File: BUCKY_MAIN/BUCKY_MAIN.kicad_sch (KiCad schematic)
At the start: 17 parts, among them J4 Conn_01x10, U1 IFX9201SG_BO, U2 IFX9201SG_BO, U3 IFX9201SG_BO, U9 PCA9548ADB

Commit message: chore: finish main board
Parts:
- removed J4: Conn_01x10, BUCKY_MAIN:CONN10_S10B-PH_JST, symbol Connector_Generic:Conn_01x10
- removed R1, R2: 4700R, Resistor_SMD:R_0402_1005Metric, symbol Device:R
- removed R3, R4, R5, R6: 10000R, Resistor_SMD:R_0402_1005Metric, symbol Device:R
- removed U1, U2, U3: IFX9201SG_BO, BUCKY_MAIN:IFX9201SG_BO, symbol BUCKY_MAIN:IFX9201SG_BO
- removed U4: ~, BUCKY_MAIN:BUCKY_POWER, symbol BUCKY_MAIN:BUCKY_POWER
- removed U5, U6, U7, U8: ~, BUCKY_MAIN:BUCKY_TOF, symbol BUCKY_MAIN:BUCKY_TOF
- removed U9: PCA9548ADB, DB24, symbol BUCKY_MULTIPLEXER:PCA9548ADB
- added A2: Arduino Mega, BUCKY_MAIN:ARDUINO_MEGA, symbol ARDUINO_MEGA:A000067
- added C1, C10, C11, C12, C2, C3, C4, C5, C6, C7, C8, C9: 10uF, Capacitor_SMD:C_0603_1608Metric, symbol Device:C
- added D10, D11, D12, D13, D14, D2, D3, D4, D5, D6, D7, D8, D9: D, Diode_SMD:D_0603_1608Metric, symbol Device:D
- added IC1, IC10, IC11, IC12, IC2, IC3, IC4, IC5, IC6, IC7, IC8, IC9: TSSP96038TR, BUCKY_MAIN:TSSP96038, symbol BUCKY_MAIN:TSSP96038TR
- added J1: Conn_01x10, BUCKY_MAIN:CONN10_S10B-PH_JST, symbol Connector_Generic:Conn_01x10
- added J2: Conn_01x16, BUCKY_MAIN:CONN_B16B-PH-SM4-TB_JST, symbol Connector_Generic:Conn_01x16
- added J3: Conn_01x02, BUCKY_MAIN:CONN_S2B-PH-K-S_JST, symbol Connector_Generic:Conn_01x02
- added J4: Conn_01x06, Connector_PinHeader_2.54mm:PinHeader_1x06_P2.54mm_Horizontal, symbol Connector_Generic:Conn_01x06
- D1: footprint (none) -> Diode_SMD:D_0603_1608Metric
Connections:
- net +5V: now also A2.5V_1 (+5V_1), A2.5V_2 (+5V_2), A2.5V_3 (+5V_3), A2.AREF, A2.VIN, D10.2 (A), D11.2 (A), D12.2 (A), D13.1 (K), D2.2 (A), D3.2 (A), D4.2 (A), D5.2 (A), D6.2 (A), D7.2 (A), D8.2 (A), D9.2 (A), J4.5 (Pin_5)
- net GND: now also A2.GND1, A2.GND2, A2.GND3, A2.GND4, A2.GND5, C1.1, C10.1, C11.1, C12.1, C2.1, C3.1, C4.1, C5.1, C6.1, C7.1, C8.1, C9.1, IC1.1 (GND), IC10.1 (GND), IC11.1 (GND), IC12.1 (GND), IC2.1 (GND), IC3.1 (GND), IC4.1 (GND), IC5.1 (GND), IC6.1 (GND), IC7.1 (GND), IC8.1 (GND), IC9.1 (GND), J1.10 (Pin_10), J3.2 (Pin_2), J4.4 (Pin_4)
- net M1_DIR: now also A2.14, J1.4 (Pin_4)
- net M1_PWM: now also A2.2, J1.3 (Pin_3)
- net M2_DIR: now also A2.15, J1.2 (Pin_2)
- net M2_PWM: now also A2.3, J1.1 (Pin_1)
- net M3_DIR: now also A2.16, J1.6 (Pin_6)
- net M3_PWM: now also A2.4, J1.5 (Pin_5)
- net SCL: now also A2.SCL, J1.8 (Pin_8)
- net SDA: now also A2.SDA, J1.7 (Pin_7)
- net at D1.1 (K): now also C1.2, IC1.3 (VS)
- new net: C3.2, D3.1 (K), IC3.3 (VS)
- new net: C8.2, D8.1 (K), IC8.3 (VS)
- new net: C4.2, D4.1 (K), IC4.3 (VS)
- new net: C10.2, D10.1 (K), IC10.3 (VS)
- new net: C2.2, D2.1 (K), IC2.3 (VS)
- new net: C11.2, D11.1 (K), IC11.3 (VS)
- new net: C6.2, D6.1 (K), IC6.3 (VS)
- new net: C9.2, D9.1 (K), IC9.3 (VS)
- new net: C5.2, D5.1 (K), IC5.3 (VS)
- new net: C7.2, D7.1 (K), IC7.3 (VS)
- new net: C12.2, D12.1 (K), IC12.3 (VS)
- new net: D14.1 (K), J3.1 (Pin_1)
- new net +3.3V: A2.3V3 (+3V3)
- new net D_A: A2.AD0, J2.10 (Pin_10)
- new net D_S0: A2.42, J2.7 (Pin_7)
- new net D_S1: A2.41, J2.9 (Pin_9)
- new net D_S2: A2.40, J2.8 (Pin_8)
- new net EN: J4.6 (Pin_6)
- new net F_A: A2.AD3, J2.12 (Pin_12)
- new net F_S0: A2.38, J2.11 (Pin_11)
- new net F_S1: A2.45, J2.6 (Pin_6)
- new net F_S2: A2.44, J2.5 (Pin_5)
- new net IR_1: A2.50, IC1.4 (OUT)
- new net IR_10: A2.13, IC10.4 (OUT)
- new net IR_11: A2.52, IC11.4 (OUT)
- new net IR_12: A2.53, IC12.4 (OUT)
- new net IR_2: A2.51, IC2.4 (OUT)
- new net IR_3: A2.48, IC3.4 (OUT)
- new net IR_4: A2.43, IC4.4 (OUT)
- new net IR_5: A2.23, IC5.4 (OUT)
- new net IR_6: A2.21, IC6.4 (OUT)
- new net IR_7: A2.5, IC7.4 (OUT)
- new net IR_8: A2.11, IC8.4 (OUT)
- new net IR_9: A2.12, IC9.4 (OUT)
- new net L_A: A2.AD1, J2.13 (Pin_13)
- new net L_S0: A2.37, J2.16 (Pin_16)
- new net L_S1: A2.36, J2.15 (Pin_15)
- new net L_S2: A2.39, J2.14 (Pin_14)
- new net RXD: A2.19, J4.3 (Pin_3)
- new net R_A: A2.AD2, J2.1 (Pin_1)
- new net R_S0: A2.49, J2.2 (Pin_2)
- new net R_S1: A2.46, J2.3 (Pin_3)
- new net R_S2: A2.47, J2.4 (Pin_4)
- new net STATE: J4.1 (Pin_1)
- new net TXD: A2.18, J4.2 (Pin_2)
- new net VIN: D13.2 (A), D14.2 (A), J1.9 (Pin_9)
- no-connect marks 12 -> 23
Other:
- note added: "BUCKY DRIVE"
- note added: "BUCKY LIGHT"
- note added: "BUCKY LIGHT POWER"
- note added: "EN"
- note added: "GND"
- note added: "HC-05"
- note added: "INFRARED SENSORS"
- note added: "MCU (ARDUINO MEGA R3)"
- note added: "PWM"
- note added: "RXD"
- note added: "STATE"
- note added: "THE DIODES ARE TO MAKE PROBING EASIER"
- note added: "TXD"
- note added: "VCC"
- note added: "WIRELESS COMMUNICATION"
- note removed: "CONNECTORS (TO BUCKY_PCB/BUCKY_IR)"
- note removed: "I2C Multiplexer Creds: Bas de Graaf"
- note removed: "MOTOR DRIVERS"
- note removed: "POWER CIRCUIT BUCKY_PCB/BUCKY_POWER"
- note removed: "TOF SENSORS (DISTANCE)"
- title: MAIN BOARD -> BUCKY MAIN

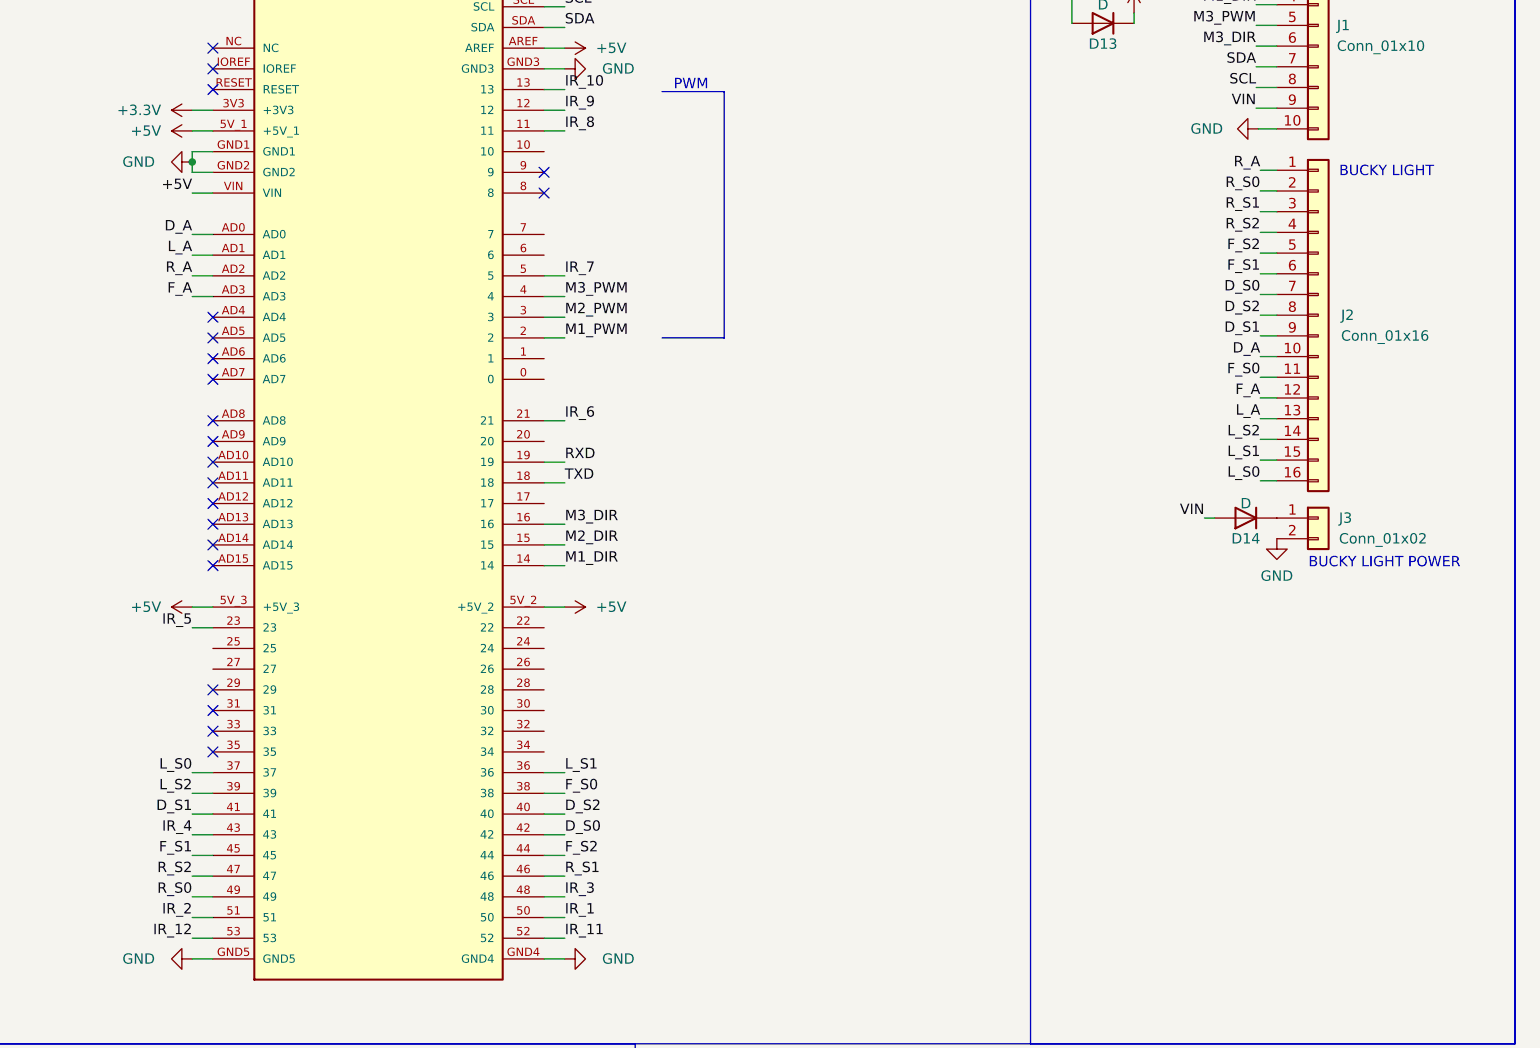
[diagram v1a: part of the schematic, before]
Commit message: chore: start on ldr instead of Q_Photo_N, interrupt instead of analog multiplexer. And a signal for front,back,left,right
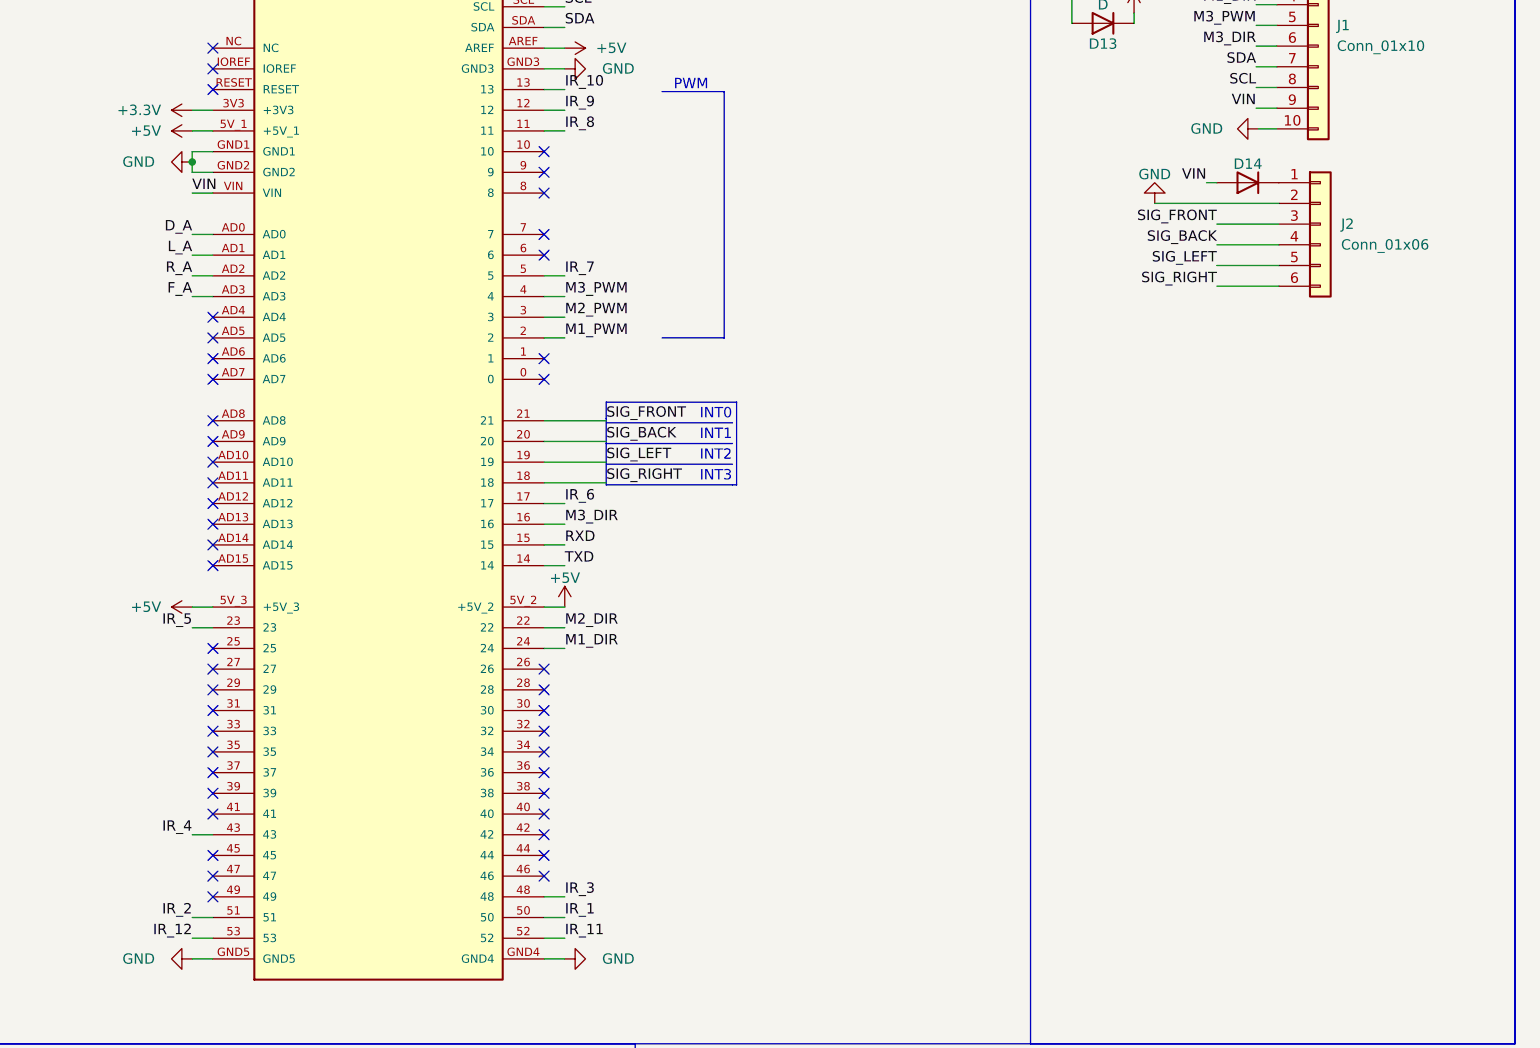
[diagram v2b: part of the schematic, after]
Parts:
- removed J2: Conn_01x16, BUCKY_MAIN:CONN_B16B-PH-SM4-TB_JST, symbol Connector_Generic:Conn_01x16
- removed J3: Conn_01x02, BUCKY_MAIN:CONN_S2B-PH-K-S_JST, symbol Connector_Generic:Conn_01x02
- added J2: Conn_01x06, BUCKY_MAIN:LIGHT_CONN, symbol Connector_Generic:Conn_01x06
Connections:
- net +5V: no longer A2.VIN
- net GND: now also J2.2 (Pin_2)
- net IR_6: now also A2.17; no longer A2.21
- net M1_DIR: now also A2.24; no longer A2.14
- net M2_DIR: now also A2.22; no longer A2.15
- net RXD: now also A2.15; no longer A2.19
- net TXD: now also A2.14; no longer A2.18
- net VIN: now also A2.VIN
- net at D14.1 (K): now also J2.1 (Pin_1)
- net SIG_BACK: now reaches A2.20
- net SIG_BACK: now also J2.4 (Pin_4)
- net D_S0: no longer names the net of A2.42
- net D_S1: no longer names the net of A2.41
- net D_S2: no longer names the net of A2.40
- net F_S0: no longer names the net of A2.38
- net F_S1: no longer names the net of A2.45
- net F_S2: no longer names the net of A2.44
- net L_S0: no longer names the net of A2.37
- net L_S1: no longer names the net of A2.36
- net L_S2: no longer names the net of A2.39
- net R_S0: no longer names the net of A2.49
- net R_S1: no longer names the net of A2.46
- net R_S2: no longer names the net of A2.47
- new net SIG_FRONT: A2.21, J2.3 (Pin_3)
- new net SIG_LEFT: A2.19, J2.5 (Pin_5)
- new net SIG_RIGHT: A2.18, J2.6 (Pin_6)
- no-connect marks 23 -> 47
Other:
- note added: "INT0"
- note added: "INT1"
- note added: "INT2"
- note added: "INT3"
- note removed: "BUCKY LIGHT"
- note removed: "BUCKY LIGHT POWER"

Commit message: finish up robot (i think)
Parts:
- removed A2: Arduino Mega, BUCKY_MAIN:ARDUINO_MEGA, symbol ARDUINO_MEGA:A000067
- removed IC1, IC10, IC11, IC12, IC2, IC3, IC4, IC5, IC6, IC7, IC8, IC9: TSSP96038TR, BUCKY_MAIN:TSSP96038, symbol BUCKY_MAIN:TSSP96038TR
- added A1: Arduino Mega, BUCKY_MAIN:ARDUINO_MEGA, symbol ARDUINO_MEGA:A000067
- added S1, S10, S11, S12, S2, S3, S4, S5, S6, S7, S8, S9: TSSP96038TR, BUCKY_MAIN:TSSP96038, symbol BUCKY_MAIN:TSSP96038TR
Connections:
- net +3.3V: now also A1.3V3 (+3V3)
- net +5V: now also A1.5V_1 (+5V_1), A1.5V_2 (+5V_2), A1.5V_3 (+5V_3), A1.AREF
- net D_A: now also A1.AD0
- net F_A: now also A1.AD3
- net GND: now also A1.GND1, A1.GND2, A1.GND3, A1.GND4, A1.GND5, S1.1 (GND), S10.1 (GND), S11.1 (GND), S12.1 (GND), S2.1 (GND), S3.1 (GND), S4.1 (GND), S5.1 (GND), S6.1 (GND), S7.1 (GND), S8.1 (GND), S9.1 (GND)
- net IR_1: now also A1.50
- net IR_10: now also A1.13
- net IR_11: now also A1.52
- net IR_12: now also A1.53, S1.4 (OUT), S10.4 (OUT), S11.4 (OUT), S12.4 (OUT), S2.4 (OUT), S3.4 (OUT), S4.4 (OUT), S5.4 (OUT), S6.4 (OUT), S7.4 (OUT), S8.4 (OUT), S9.4 (OUT)
- net IR_2: now also A1.51
- net IR_3: now also A1.48
- net IR_4: now also A1.43
- net IR_5: now also A1.23
- net IR_6: now also A1.17
- net IR_7: now also A1.5
- net IR_8: now also A1.11
- net IR_9: now also A1.12
- net L_A: now also A1.AD1
- net M1_DIR: now also A1.24
- net M1_PWM: now also A1.2
- net M2_DIR: now also A1.22
- net M2_PWM: now also A1.3
- net M3_DIR: now also A1.16
- net M3_PWM: now also A1.4
- net RXD: now also A1.15
- net R_A: now also A1.AD2
- net SCL: now also A1.SCL
- net SDA: now also A1.SDA
- net SIG_BACK: now also A1.20
- net SIG_FRONT: now also A1.21
- net SIG_LEFT: now also A1.19
- net SIG_RIGHT: now also A1.18
- net TXD: now also A1.14
- net VIN: now also A1.VIN
- net at C3.2, D3.1 (K): now also S3.3 (VS)
- net at C8.2, D8.1 (K): now also S8.3 (VS)
- net at C4.2, D4.1 (K): now also S4.3 (VS)
- net at C10.2, D10.1 (K): now also S10.3 (VS)
- net at C2.2, D2.1 (K): now also S2.3 (VS)
- net at C11.2, D11.1 (K): now also S11.3 (VS)
- net at C6.2, D6.1 (K): now also S6.3 (VS)
- net at C9.2, D9.1 (K): now also S9.3 (VS)
- net at C5.2, D5.1 (K): now also S5.3 (VS)
- net at C7.2, D7.1 (K): now also S7.3 (VS)
- net at C1.2, D1.1 (K): now also S1.3 (VS)
- net at C12.2, D12.1 (K): now also S12.3 (VS)
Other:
- note added: "BUCKY LIGHT"
- moved on the sheet: D13, D14, J1, J2

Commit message: chore: make all PCBs from 2 layers to 4 layers
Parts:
- C1, C10, C11, C12, C2, C3, C4, C5, C6, C7, C8, C9: footprint Capacitor_SMD:C_0603_1608Metric -> Capacitor_SMD:C_0805_2012Metric
- D1, D10, D11, D12, D13, D14, D2, D3, D4, D5, D6, D7, D8, D9: footprint Diode_SMD:D_0603_1608Metric -> Diode_SMD:D_0805_2012Metric
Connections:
- net IR_1: now also S1.4 (OUT)
- net IR_10: now also S10.4 (OUT)
- net IR_11: now also S11.4 (OUT)
- net IR_12: no longer S1.4 (OUT), S10.4 (OUT), S11.4 (OUT), S2.4 (OUT), S3.4 (OUT), S4.4 (OUT), S5.4 (OUT), S6.4 (OUT), S7.4 (OUT), S8.4 (OUT), S9.4 (OUT)
- net IR_2: now also S2.4 (OUT)
- net IR_3: now also S3.4 (OUT)
- net IR_4: now also S4.4 (OUT)
- net IR_5: now also S5.4 (OUT)
- net IR_6: now also S6.4 (OUT)
- net IR_7: now also S7.4 (OUT)
- net IR_8: now also S8.4 (OUT)
- net IR_9: now also S9.4 (OUT)
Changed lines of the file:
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@@
 	(title_block
 		(title "BUCKY MAIN")
-		(date "2024-05-07")
+		(date "2024-09-11")
 		(rev "V1")
 		(company "koen1711")
@@
 		)
 	)
-	(label "IR_12"
+	(label "IR_8"
 		(at 85.09 101.6 180)
 		(fields_autoplaced yes)
@@
 		)
 	)
-	(label "IR_12"
+	(label "IR_10"
 		(at 134.62 52.07 180)
 		(fields_autoplaced yes)
@@
 		)
 	)
-	(label "IR_12"
+	(label "IR_4"
 		(at 36.83 101.6 180)
 		(fields_autoplaced yes)
@@
 		)
 	)
-	(label "IR_12"
+	(label "IR_2"
 		(at 36.83 52.07 180)
 		(fields_autoplaced yes)
@@
 		)
 	)
-	(label "IR_12"
+	(label "IR_1"
 		(at 36.83 27.94 180)
 		(fields_autoplaced yes)
@@
 		)
 	)
-	(label "IR_12"
+	(label "IR_6"
 		(at 85.09 52.07 180)
 		(fields_autoplaced yes)
@@
 		)
 	)
-	(label "IR_12"
+	(label "IR_7"
 		(at 85.09 76.2 180)
 		(fields_autoplaced yes)
@@
 		)
 	)
-	(label "IR_12"
+	(label "IR_11"
 		(at 134.62 76.2 180)
 		(fields_autoplaced yes)
@@
 		)
 	)
-	(label "IR_12"
+	(label "IR_5"
 		(at 85.09 27.94 180)
 		(fields_autoplaced yes)
@@
 		)
 	)
-	(label "IR_12"
+	(label "IR_9"
 		(at 134.62 27.94 180)
 		(fields_autoplaced yes)
@@
 		)
 	)
-	(label "IR_12"
+	(label "IR_3"
 		(at 36.83 76.2 180)
 		(fields_autoplaced yes)
@@
 			)
 		)
-		(property "Footprint" "Capacitor_SMD:C_0603_1608Metric"
+		(property "Footprint" "Capacitor_SMD:C_0805_2012Metric"
 			(at 75.2348 49.53 0)
 			(effects
@@
 			)
 		)
-		(property "Footprint" "Capacitor_SMD:C_0603_1608Metric"
+		(property "Footprint" "Capacitor_SMD:C_0805_2012Metric"
 			(at 26.9748 73.66 0)
 			(effects
@@
 			)
 		)
-		(property "Footprint" "Capacitor_SMD:C_0603_1608Metric"
+		(property "Footprint" "Capacitor_SMD:C_0805_2012Metric"
 			(at 75.2348 73.66 0)
 			(effects
@@
 			)
 		)
-		(property "Footprint" "Diode_SMD:D_0603_1608Metric"
+		(property "Footprint" "Diode_SMD:D_0805_2012Metric"
 			(at 69.85 99.06 0)
 			(effects
@@
 			)
 		)
-		(property "Footprint" "Diode_SMD:D_0603_1608Metric"
+		(property "Footprint" "Diode_SMD:D_0805_2012Metric"
 			(at 69.85 49.53 0)
 			(effects
@@
 			)
 		)
-		(property "Footprint" "Diode_SMD:D_0603_1608Metric"
+		(property "Footprint" "Diode_SMD:D_0805_2012Metric"
 			(at 119.38 73.66 0)
 			(effects
@@
 			)
 		)
-		(property "Footprint" "Diode_SMD:D_0603_1608Metric"
+		(property "Footprint" "Diode_SMD:D_0805_2012Metric"
 			(at 21.59 25.4 0)
 			(effects
@@
 			)
 		)
-		(property "Footprint" "Capacitor_SMD:C_0603_1608Metric"
+		(property "Footprint" "Capacitor_SMD:C_0805_2012Metric"
 			(at 124.7648 73.66 0)
 			(effects
@@
 			)
 		)
-		(property "Footprint" "Capacitor_SMD:C_0603_1608Metric"
+		(property "Footprint" "Capacitor_SMD:C_0805_2012Metric"
 			(at 75.2348 25.4 0)
 			(effects
@@
 			)
 		)
-		(property "Footprint" "Capacitor_SMD:C_0603_1608Metric"
+		(property "Footprint" "Capacitor_SMD:C_0805_2012Metric"
 			(at 124.7648 49.53 0)
 			(effects
@@
 			)
 		)
-		(property "Footprint" "Diode_SMD:D_0603_1608Metric"
+		(property "Footprint" "Diode_SMD:D_0805_2012Metric"
 			(at 69.85 25.4 0)
 			(effects
@@
 			)
 		)
-		(property "Footprint" "Capacitor_SMD:C_0603_1608Metric"
+		(property "Footprint" "Capacitor_SMD:C_0805_2012Metric"
 			(at 124.7648 99.06 0)
 			(effects
@@
 			)
 		)
-		(property "Footprint" "Capacitor_SMD:C_0603_1608Metric"
+		(property "Footprint" "Capacitor_SMD:C_0805_2012Metric"
 			(at 26.9748 25.4 0)
 			(effects
@@
 			)
 		)
-		(property "Footprint" "Diode_SMD:D_0603_1608Metric"
+		(property "Footprint" "Diode_SMD:D_0805_2012Metric"
 			(at 69.85 73.66 0)
 			(effects
@@
 			)
 		)
-		(property "Footprint" "Diode_SMD:D_0603_1608Metric"
+		(property "Footprint" "Diode_SMD:D_0805_2012Metric"
 			(at 166.37 39.37 0)
 			(effects
@@
 			)
 		)
-		(property "Footprint" "Capacitor_SMD:C_0603_1608Metric"
+		(property "Footprint" "Capacitor_SMD:C_0805_2012Metric"
 			(at 26.9748 99.06 0)
 			(effects
@@
 			)
 		)
-		(property "Footprint" "Capacitor_SMD:C_0603_1608Metric"
+		(property "Footprint" "Capacitor_SMD:C_0805_2012Metric"
 			(at 124.7648 25.4 0)
 			(effects
@@
 			)
 		)
-		(property "Footprint" "Capacitor_SMD:C_0603_1608Metric"
+		(property "Footprint" "Capacitor_SMD:C_0805_2012Metric"
 			(at 75.2348 99.06 0)
 			(effects
@@
 			)
 		)
-		(property "Footprint" "Diode_SMD:D_0603_1608Metric"
+		(property "Footprint" "Diode_SMD:D_0805_2012Metric"
 			(at 21.59 49.53 0)
 			(effects
@@
 			)
 		)
-		(property "Footprint" "Diode_SMD:D_0603_1608Metric"
+		(property "Footprint" "Diode_SMD:D_0805_2012Metric"
 			(at 119.38 49.53 0)
 			(effects
@@
 			)
 		)
-		(property "Footprint" "Diode_SMD:D_0603_1608Metric"
+		(property "Footprint" "Diode_SMD:D_0805_2012Metric"
 			(at 21.59 73.66 0)
 			(effects
@@
 			)
 		)
-		(property "Footprint" "Capacitor_SMD:C_0603_1608Metric"
+		(property "Footprint" "Capacitor_SMD:C_0805_2012Metric"
 			(at 26.9748 49.53 0)
 			(effects
@@
 			)
 		)
-		(property "Footprint" "Diode_SMD:D_0603_1608Metric"
+		(property "Footprint" "Diode_SMD:D_0805_2012Metric"
 			(at 119.38 25.4 0)
 			(effects
@@
 			)
 		)
-		(property "Footprint" "Diode_SMD:D_0603_1608Metric"
+		(property "Footprint" "Diode_SMD:D_0805_2012Metric"
 			(at 119.38 99.06 0)
 			(effects
@@
 			)
 		)
-		(property "Footprint" "Diode_SMD:D_0603_1608Metric"
+		(property "Footprint" "Diode_SMD:D_0805_2012Metric"
 			(at 21.59 99.06 0)
 			(effects
@@
 			)
 		)
-		(property "Footprint" "Diode_SMD:D_0603_1608Metric"
+		(property "Footprint" "Diode_SMD:D_0805_2012Metric"
 			(at 186.69 67.31 0)
 			(effects
